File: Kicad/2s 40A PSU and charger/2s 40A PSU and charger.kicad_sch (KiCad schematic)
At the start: 0 parts

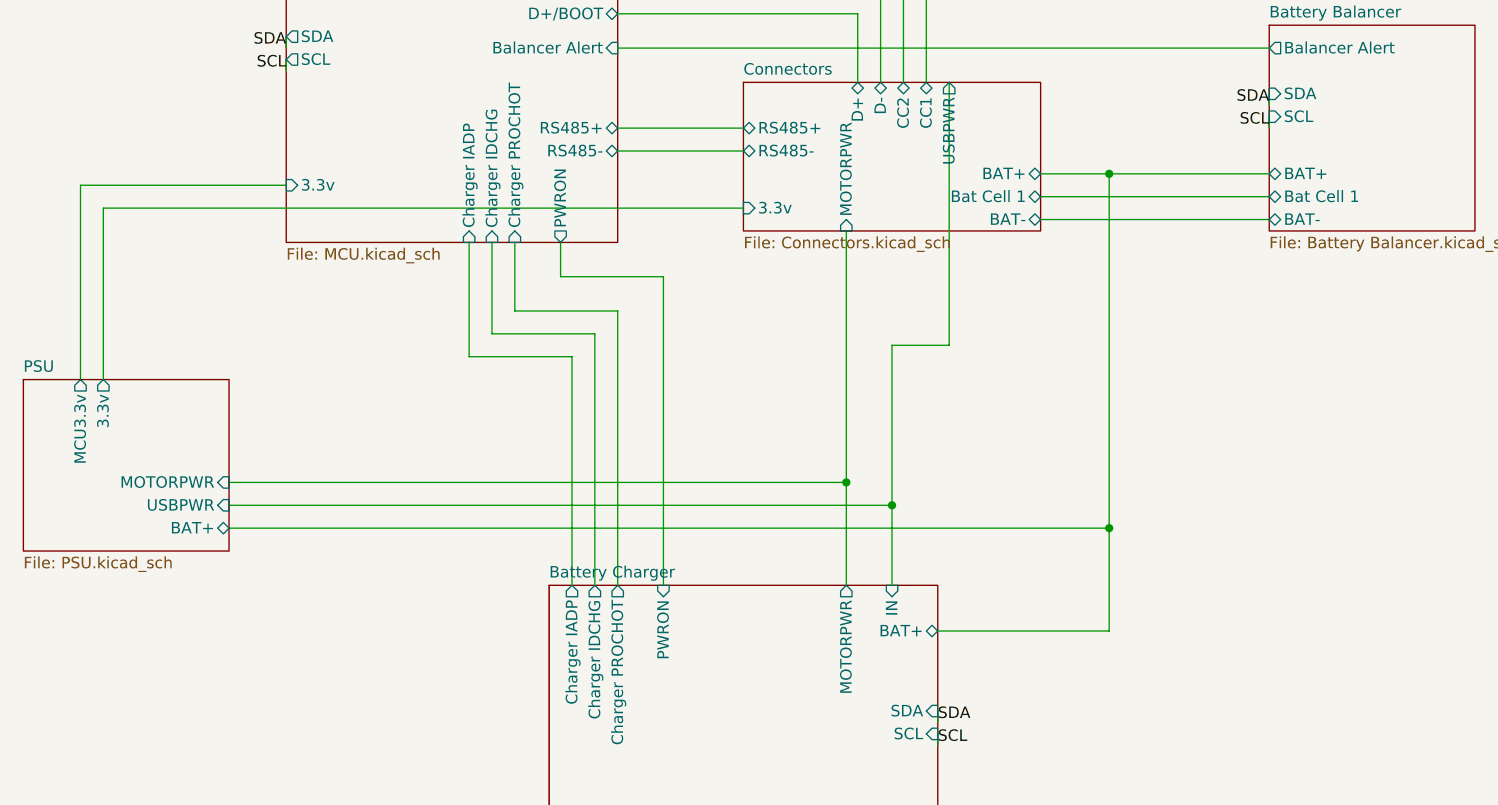
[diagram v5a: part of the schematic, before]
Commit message: Added use of Net Class Directives to speed up routing
I don't have to manually change wire sizes now
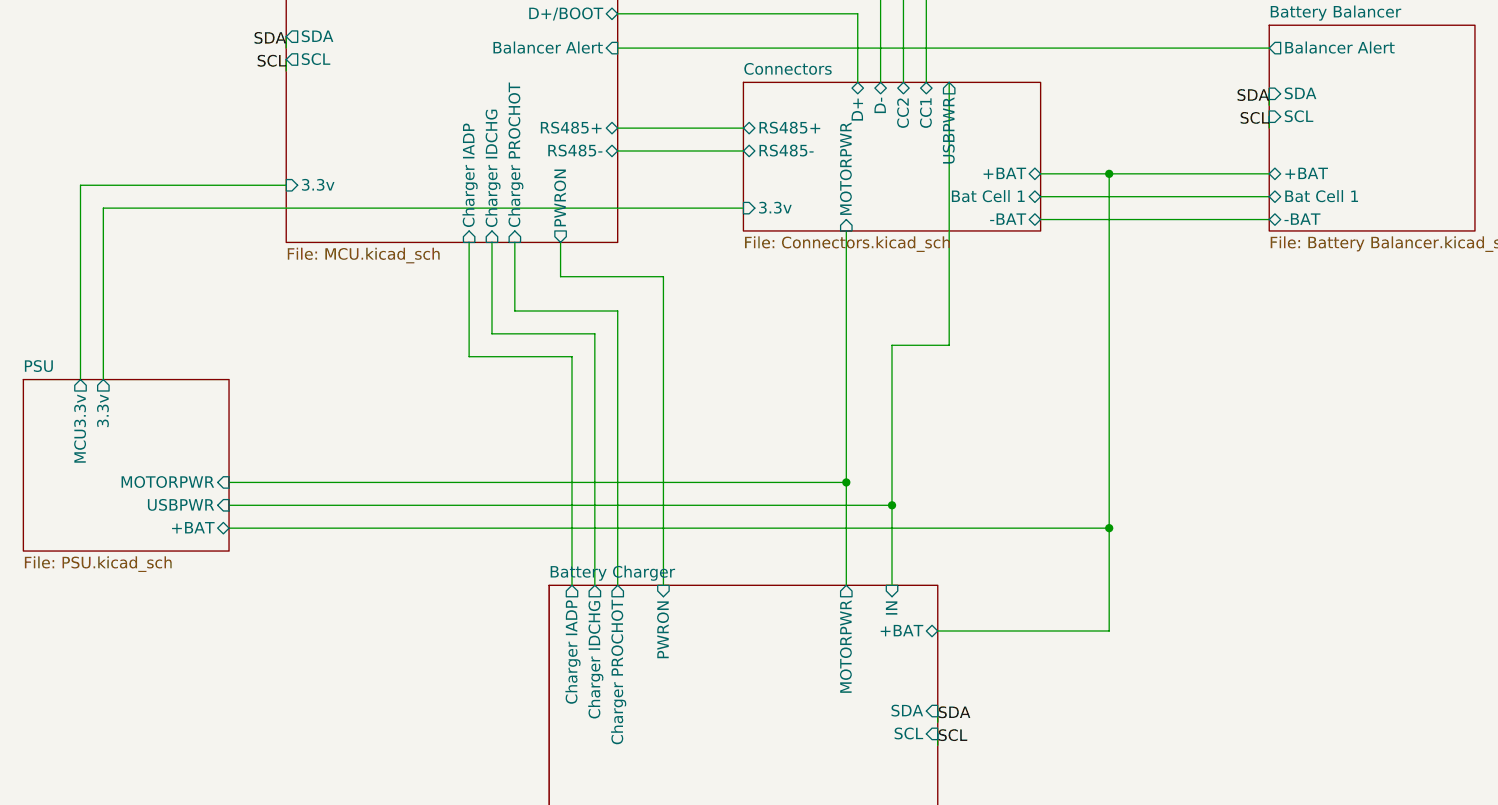
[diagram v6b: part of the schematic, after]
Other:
- sheet Battery Balancer ports: added +BAT, -BAT; removed BAT+, BAT-
- sheet Battery Charger ports: added +BAT; removed BAT+
- sheet Connectors ports: added +BAT, -BAT; removed BAT+, BAT-
- sheet PSU ports: added +BAT; removed BAT+
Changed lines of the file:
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@@
 			)
 		)
-		(pin "BAT+" bidirectional
+		(pin "+BAT" bidirectional
 			(at 181.61 80.01 0)
 			(effects
@@
 			)
 		)
-		(pin "BAT-" bidirectional
+		(pin "-BAT" bidirectional
 			(at 181.61 85.09 0)
 			(effects
@@
 			)
 		)
-		(pin "BAT+" bidirectional
+		(pin "+BAT" bidirectional
 			(at 170.18 130.81 0)
 			(effects
@@
 			)
 		)
-		(pin "BAT-" bidirectional
+		(pin "-BAT" bidirectional
 			(at 207.01 85.09 180)
 			(effects
@@
 			)
 		)
-		(pin "BAT+" bidirectional
+		(pin "+BAT" bidirectional
 			(at 207.01 80.01 180)
 			(effects
@@
 			)
 		)
-		(pin "BAT+" bidirectional
+		(pin "+BAT" bidirectional
 			(at 91.44 119.38 0)
 			(effects

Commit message: Updated Sheet Properties
My author name is now in there, and I've added the proper project name.
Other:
- title: (none) -> CACKLE 2s 40A PSU & Charger
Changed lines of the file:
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@@
 	(paper "A4")
 	(title_block
-		(date "2024-11-28")
-		(rev "V1 Alpha")
+		(title "CACKLE 2s 40A PSU & Charger")
+		(date "2024-12-01")
+		(rev "V1")
+		(comment 1 "Author: Asher Edwards")
 	)
 	(junction

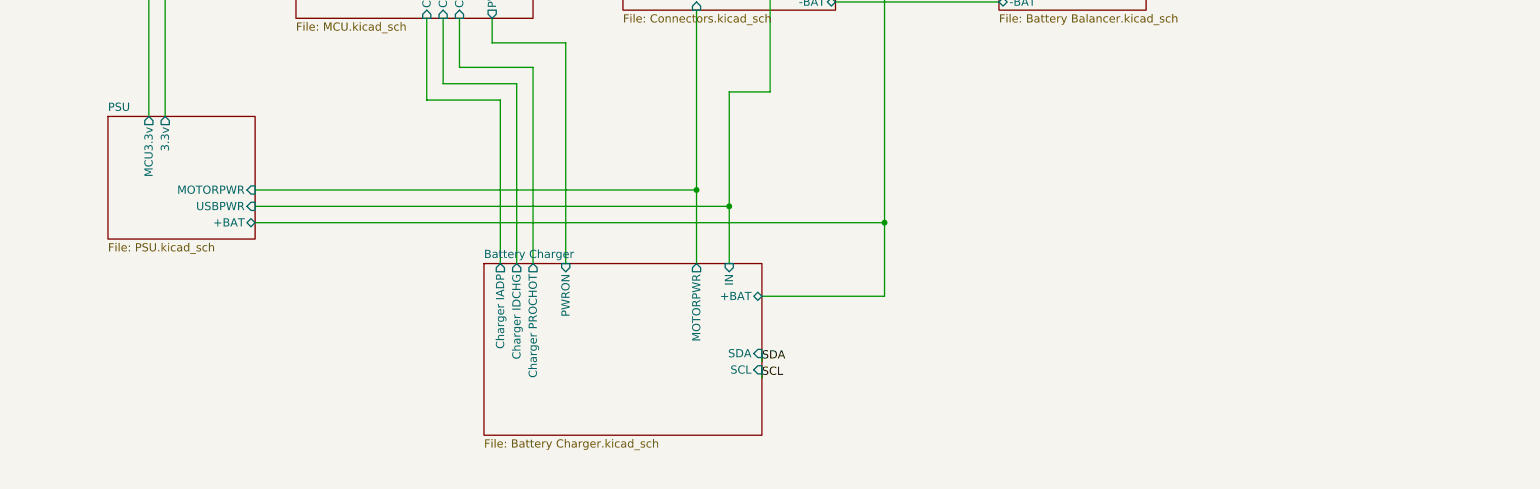
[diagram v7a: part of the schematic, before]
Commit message: Merged Always on PWR for multiple devices
The diode OR and the 10 ohm resistor are now shared between the MCU and the battery charger
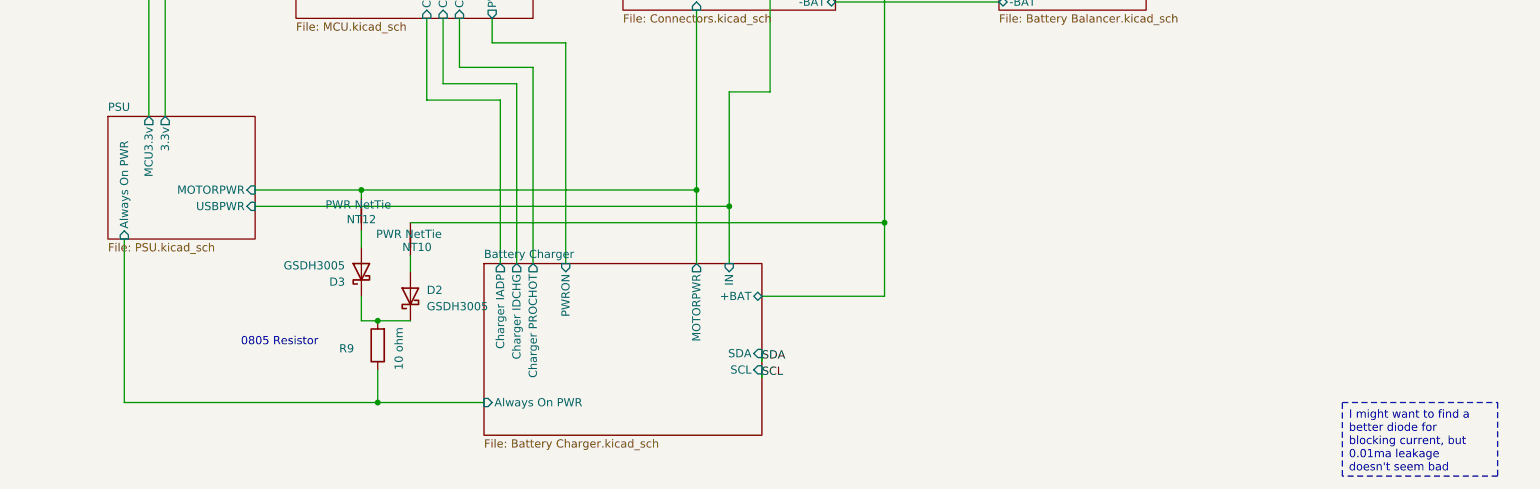
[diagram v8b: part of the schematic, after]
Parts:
- added D2, D3: GSDH3005, Diode_SMD:D_0402_1005Metric, symbol Device:D_Schottky
- added NT10, NT12: PWR NetTie, custom_Connector:NetTie-2_SMD_Pad0.28mm, symbol Device:NetTie_2
- added R9: 10 ohm, Resistor_SMD:R_0805_2012Metric, symbol Device:R
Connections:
- net Battery Balancer/+BAT: now also NT10.2
- net Battery Charger/MOTORPWR: now also NT12.2
- new net: D2.1 (K), D3.1 (K), R9.2
- new net: D3.2 (A), NT12.1
- new net: D2.2 (A), NT10.1
- new net Battery Charger/Always On PWR: R9.1
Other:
- sheet Battery Charger ports: added Always On PWR; removed none
- sheet PSU ports: added Always On PWR; removed +BAT
- note added: "0805 Resistor"
